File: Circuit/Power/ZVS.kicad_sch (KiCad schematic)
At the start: 18 parts

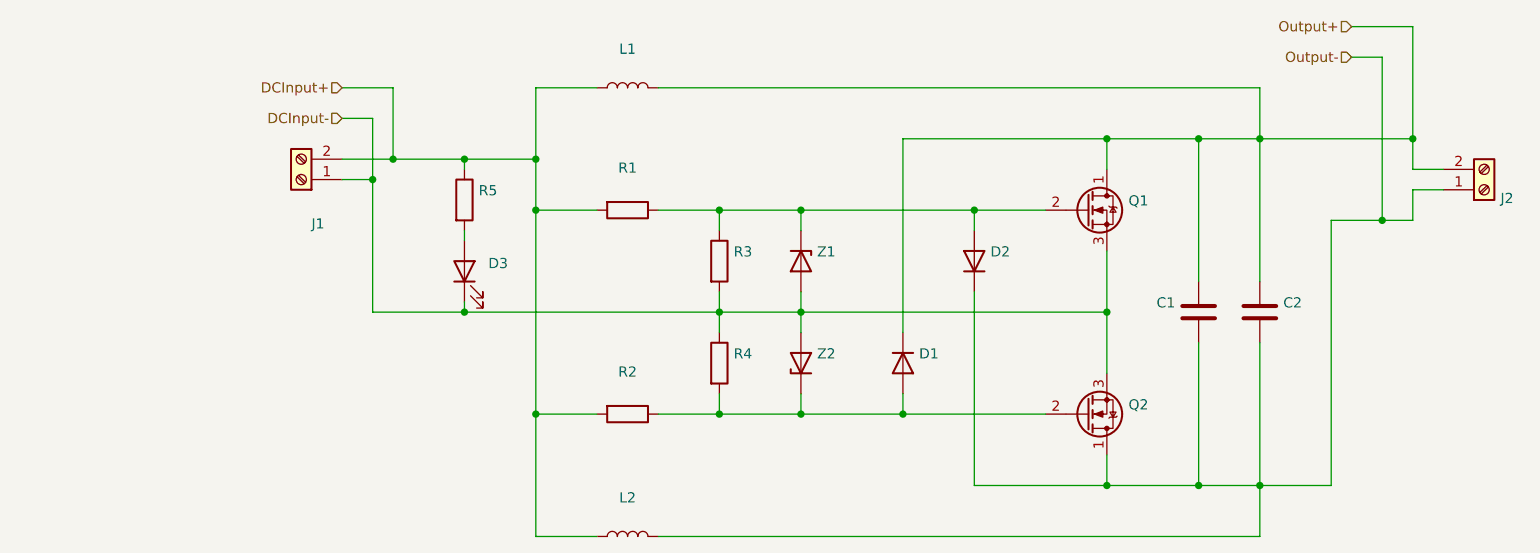
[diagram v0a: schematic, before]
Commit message: [Circuit] High frequency ZVS module with gate driver
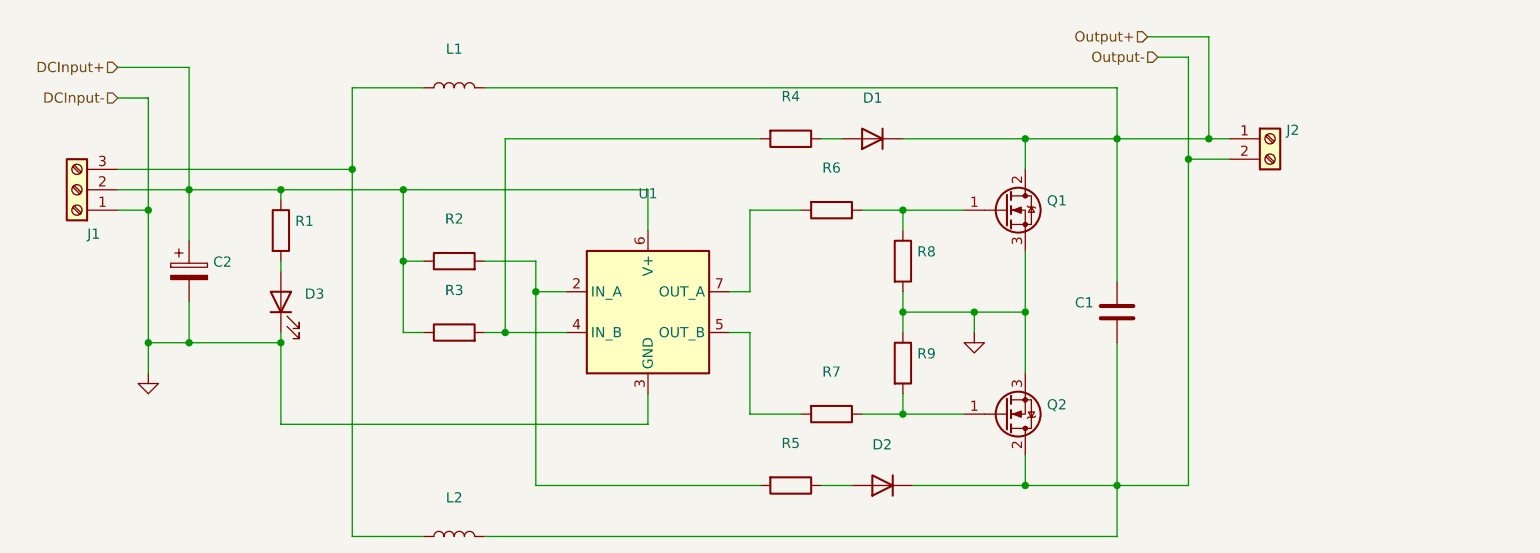
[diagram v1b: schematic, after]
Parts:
- removed C2: (no value), symbol Device:C
- removed R1: (no value), symbol Device:R
- removed Z1, Z2: (no value), symbol Diode:1N47xxA
- added C2: (no value), symbol Device:C_Polarized
- added R3, R4, R5, R6, R7: (no value), symbol Device:R
- added U1: (no value), symbol Driver_FET:EL7202CN
- J1: symbol Connector:Screw_Terminal_01x02 -> Connector:Screw_Terminal_01x03
- Q1, Q2: symbol Device:Q_NMOS_DGS -> Device:Q_NMOS_GDS
- renumbered R5 to R1, R3 to R8, R4 to R9
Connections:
- net DCInput+: now also R2.1, C2.1, R3.1, U1.6 (V+); no longer L1.1, L2.1, R2.2
- net Output+: now also J2.1 (Pin_1), Q1.2 (D); no longer J2.2 (Pin_2), Q1.1 (D)
- net Output-: now also J2.2 (Pin_2), Q2.2 (D); no longer J2.1 (Pin_1), Q2.1 (D)
- net DCInput- renamed GND
- net GND: now also C2.2, U1.3 (GND)
- new net: J1.3 (Pin_3), L1.1, L2.1
- new net: Q1.1 (G), R6.1, R8.1
- new net: Q2.1 (G), R7.1, R9.2
- new net: D1.2 (A), R4.1
- new net: D2.2 (A), R5.1
- new net: R2.2, R5.2, U1.2 (IN_A)
- new net: R3.2, R4.2, U1.4 (IN_B)
- new net: R7.2, U1.5 (OUT_B)
- new net: R6.2, U1.7 (OUT_A)
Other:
- moved on the sheet: C1, D1, D2, D3, J2, L1, L2, Q1, Q2, R1, R8, R9
